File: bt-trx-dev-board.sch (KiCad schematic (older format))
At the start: 10 parts, among them J2 PTT_BUTTON, J3 AudioJack2, J4 PTT_SELECT, J5 RJ45, J6 ENABLE_PTT_IN, U1 SILabs_WT32i

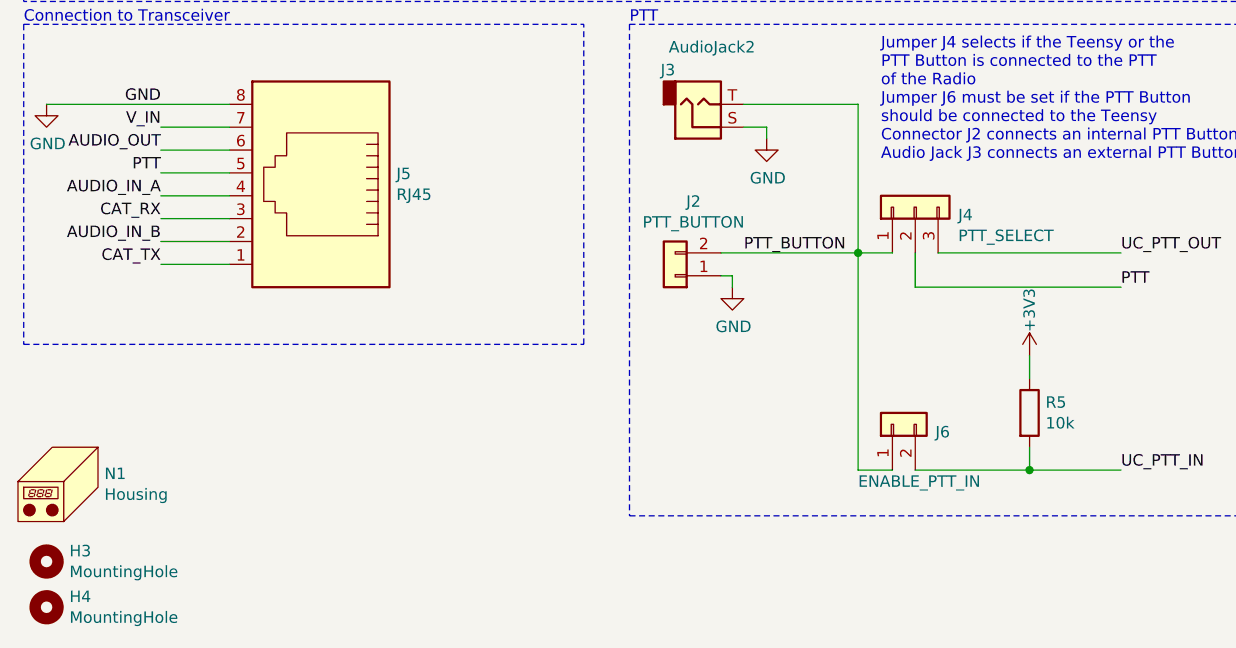
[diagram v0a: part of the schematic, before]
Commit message: Assigned Pins to ESP32 and removed Teensy [#1]
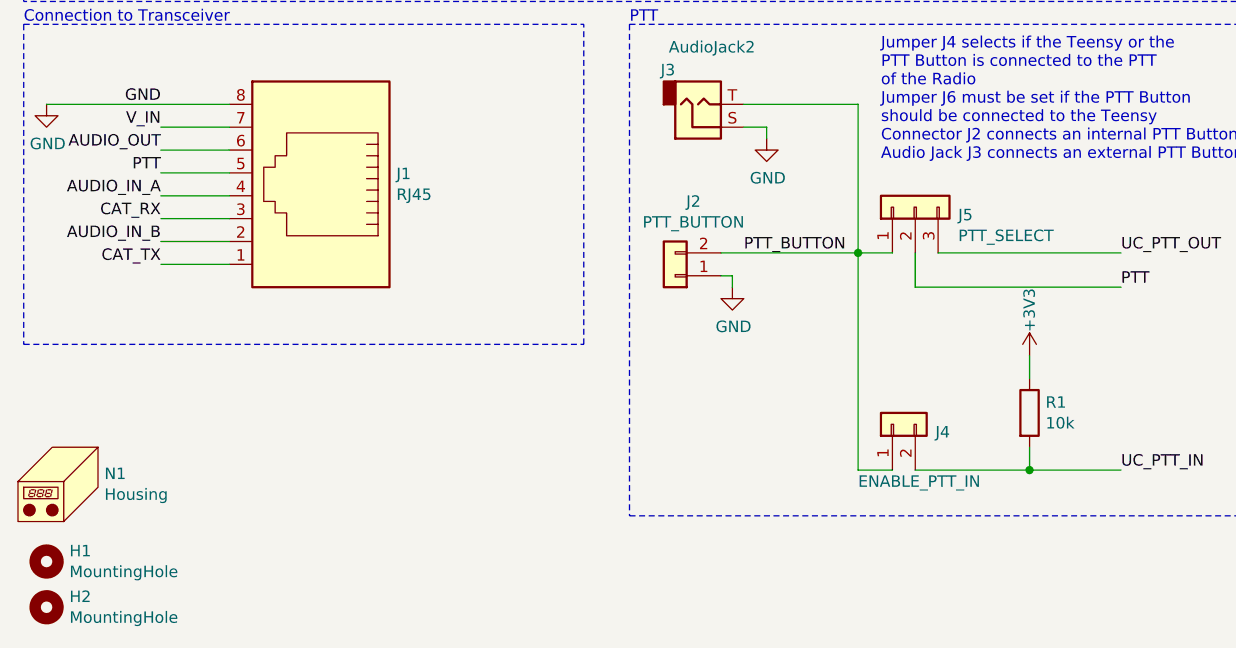
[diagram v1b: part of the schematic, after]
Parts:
- renumbered H3 to H1, H4 to H2, J5 to J1, J6 to J4, J4 to J5, R5 to R1
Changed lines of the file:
@@
 NoConn ~ 3950 3850
 $Comp
-L power:GND #PWR03
+L power:GND #PWR04
 U 1 1 5C05D773
 P 3150 3950
-F 0 "#PWR03" H 3150 3700 50  0001 C CNN
+F 0 "#PWR04" H 3150 3700 50  0001 C CNN
 F 1 "GND" H 3155 3777 50  0000 C CNN
 F 2 "" H 3150 3950 50  0001 C CNN
@@
 $EndComp
 $Comp
-L power:GND #PWR01
+L power:GND #PWR02
 U 1 1 5C05D830
 P 2600 1850
-F 0 "#PWR01" H 2600 1600 50  0001 C CNN
+F 0 "#PWR02" H 2600 1600 50  0001 C CNN
 F 1 "GND" H 2605 1677 50  0000 C CNN
 F 2 "" H 2600 1850 50  0001 C CNN
@@
 Connection ~ 2700 1850
 $Comp
-L power:GND #PWR04
+L power:GND #PWR07
 U 1 1 5C06905F
 P 4800 2550
-F 0 "#PWR04" H 4800 2300 50  0001 C CNN
+F 0 "#PWR07" H 4800 2300 50  0001 C CNN
 F 1 "GND" H 4805 2377 50  0000 C CNN
 F 2 "" H 4800 2550 50  0001 C CNN
@@
 MIC_BIAS
 $Comp
-L power:+3V3 #PWR02
+L power:+3V3 #PWR03
 U 1 1 5C08557D
 P 2750 3350
-F 0 "#PWR02" H 2750 3200 50  0001 C CNN
+F 0 "#PWR03" H 2750 3200 50  0001 C CNN
 F 1 "+3V3" H 2765 3523 50  0000 C CNN
 F 2 "" H 2750 3350 50  0001 C CNN
@@
 	4650 2750 4800 2750
 $Comp
-L power:+3V3 #PWR05
+L power:+3V3 #PWR08
 U 1 1 5C099E67
 P 4800 2750
-F 0 "#PWR05" H 4800 2600 50  0001 C CNN
+F 0 "#PWR08" H 4800 2600 50  0001 C CNN
 F 1 "+3V3" H 4815 2923 50  0000 C CNN
 F 2 "" H 4800 2750 50  0001 C CNN
@@
 WT32_ONOFF_FROM_UC
 $Comp
-L power:GND #PWR06
+L power:GND #PWR09
 U 1 1 5C1C6304
 P 4800 3350
-F 0 "#PWR06" H 4800 3100 50  0001 C CNN
+F 0 "#PWR09" H 4800 3100 50  0001 C CNN
 F 1 "GND" H 4805 3177 50  0000 C CNN
 F 2 "" H 4800 3350 50  0001 C CNN
@@
 AUDIO_IN_B
 $Comp
-L power:GND #PWR09
+L power:GND #PWR05
 U 1 1 5C0EA10B
 P 3800 5950
-F 0 "#PWR09" H 3800 5700 50  0001 C CNN
+F 0 "#PWR05" H 3800 5700 50  0001 C CNN
 F 1 "GND" H 3805 5777 50  0000 C CNN
 F 2 "" H 3800 5950 50  0001 C CNN
@@
 $EndComp
 $Comp
-L Mechanical:MountingHole H3
+L Mechanical:MountingHole H1
 U 1 1 5C071389
 P 800 7150
-F 0 "H3" H 900 7196 50  0000 L CNN
+F 0 "H1" H 900 7196 50  0000 L CNN
 F 1 "MountingHole" H 900 7105 50  0000 L CNN
 F 2 "MountingHole:MountingHole_3.2mm_M3_DIN965" H 800 7150 50  0001 C CNN
@@
 $EndComp
 $Comp
-L Mechanical:MountingHole H4
+L Mechanical:MountingHole H2
 U 1 1 5C0713CD
 P 800 7350
-F 0 "H4" H 900 7396 50  0000 L CNN
+F 0 "H2" H 900 7396 50  0000 L CNN
 F 1 "MountingHole" H 900 7305 50  0000 L CNN
 F 2 "MountingHole:MountingHole_3.2mm_M3_DIN965" H 800 7350 50  0001 C CNN
@@
 	8850 800  8750 800
 $Comp
-L power:GND #PWR011
+L power:GND #PWR013
 U 1 1 5C781CAB
 P 8650 1850
-F 0 "#PWR011" H 8650 1600 50  0001 C CNN
+F 0 "#PWR013" H 8650 1600 50  0001 C CNN
 F 1 "GND" H 8655 1677 50  0000 C CNN
 F 2 "" H 8650 1850 50  0001 C CNN
@@
 	8650 1750 8650 1850
 $Comp
-L power:GND #PWR07
+L power:GND #PWR010
 U 1 1 5C783418
 P 4850 1650
-F 0 "#PWR07" H 4850 1400 50  0001 C CNN
+F 0 "#PWR010" H 4850 1400 50  0001 C CNN
 F 1 "GND" H 4855 1477 50  0000 C CNN
 F 2 "" H 4850 1650 50  0001 C CNN
@@
 $EndComp
 $Comp
-L power:GND #PWR08
+L power:GND #PWR011
 U 1 1 5C78347E
 P 4850 2150
-F 0 "#PWR08" H 4850 1900 50  0001 C CNN
+F 0 "#PWR011" H 4850 1900 50  0001 C CNN
 F 1 "GND" H 4855 1977 50  0000 C CNN
 F 2 "" H 4850 2150 50  0001 C CNN
@@
 CAT_RX
 $Comp
-L Connector_Generic:Conn_01x03 J4
+L Connector_Generic:Conn_01x03 J5
 U 1 1 5C7B53A0
 P 4600 5600
-F 0 "J4" V 4566 5412 50  0000 R CNN
+F 0 "J5" V 4566 5412 50  0000 R CNN
 F 1 "PTT_SELECT" V 4475 5412 50  0000 R CNN
 F 2 "Connector_PinHeader_2.54mm:PinHeader_1x03_P2.54mm_Vertical" H 4600 5600 50  0001 C CNN
@@
 	4350 5800 4500 5800
 $Comp
-L power:GND #PWR010
+L power:GND #PWR06
 U 1 1 5C7A36F0
 P 3950 5300
-F 0 "#PWR010" H 3950 5050 50  0001 C CNN
+F 0 "#PWR06" H 3950 5050 50  0001 C CNN
 F 1 "GND" H 3955 5127 50  0000 C CNN
 F 2 "" H 3950 5300 50  0001 C CNN
@@
 	4350 5150 4350 5800
 $Comp
-L power:GND #PWR012
+L power:GND #PWR01
 U 1 1 5C038459
 P 800 5150
-F 0 "#PWR012" H 800 4900 50  0001 C CNN
+F 0 "#PWR01" H 800 4900 50  0001 C CNN
 F 1 "GND" H 805 4977 50  0000 C CNN
 F 2 "" H 800 5150 50  0001 C CNN
@@
 	8850 900  8750 900
 $Comp
-L Connector:RJ45 J5
+L Connector:RJ45 J1
 U 1 1 5C7A0AB1
 P 2000 5550
-F 0 "J5" H 1670 5646 50  0000 R CNN
+F 0 "J1" H 1670 5646 50  0000 R CNN
 F 1 "RJ45" H 1670 5555 50  0000 R CNN
 F 2 "Connector_RJ:RJ45_Amphenol_54602-x08_Horizontal" V 2000 5575 50  0001 C CNN
@@
 	2850 1750 2500 1750
 $Comp
-L power:+3V3 #PWR0101
+L power:+3V3 #PWR012
 U 1 1 5CD1BCEE
 P 5100 6250
-AR Path="/5CD1BCEE" Ref="#PWR0101"  Part="1"
+AR Path="/5CD1BCEE" Ref="#PWR012"  Part="1"
 AR Path="/5C10B93A/5CD1BCEE" Ref="#PWR?"  Part="1"
-F 0 "#PWR0101" H 5100 6100 50  0001 C CNN
+F 0 "#PWR012" H 5100 6100 50  0001 C CNN
 F 1 "+3V3" V 5100 6450 50  0000 C CNN
 F 2 "" H 5100 6250 50  0001 C CNN
@@
 $EndComp
 $Comp
-L Device:R R5
+L Device:R R1
 U 1 1 5CD1BCF6
 P 5100 6500
-AR Path="/5CD1BCF6" Ref="R5"  Part="1"
+AR Path="/5CD1BCF6" Ref="R1"  Part="1"
 AR Path="/5C10B93A/5CD1BCF6" Ref="R?"  Part="1"
-F 0 "R5" H 5170 6546 50  0000 L CNN
+F 0 "R1" H 5170 6546 50  0000 L CNN
 F 1 "10k" H 5170 6455 50  0000 L CNN
 F 2 "Resistor_SMD:R_0805_2012Metric_Pad1.15x1.40mm_HandSolder" V 5030 6500 50  0001 C CNN
@@
 P 4500 6550
 AR Path="/5C10B93A/5CD1BD02" Ref="J?"  Part="1"
-AR Path="/5CD1BD02" Ref="J6"  Part="1"
-F 0 "J6" V 4466 6362 50  0000 R CNN
+AR Path="/5CD1BD02" Ref="J4"  Part="1"
+F 0 "J4" V 4466 6362 50  0000 R CNN
 F 1 "ENABLE_PTT_IN" V 4250 6700 50  0000 R CNN
 F 2 "Connector_PinHeader_2.54mm:PinHeader_1x02_P2.54mm_Vertical" H 4500 6550 50  0001 C CNN

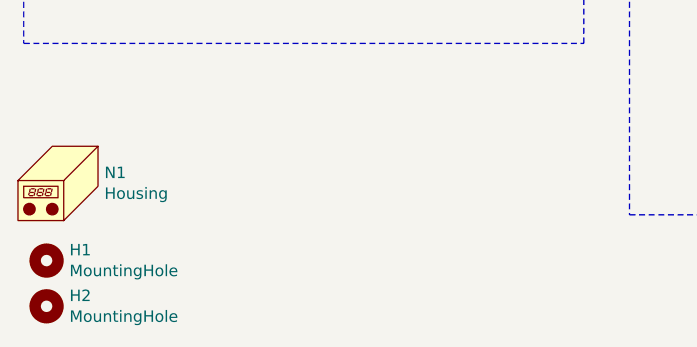
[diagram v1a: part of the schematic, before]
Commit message: Continued v4 [#1]
*removed all v3 stuff
* Resized board to max case size
* First deratsnesting
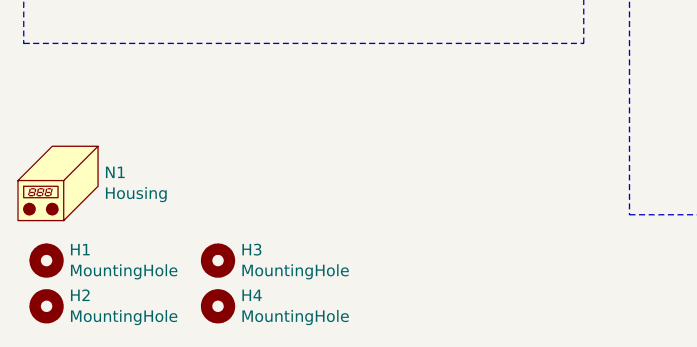
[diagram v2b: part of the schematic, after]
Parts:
- added H3, H4: MountingHole, MountingHole:MountingHole_3.2mm_M3_DIN965, symbol Mechanical:MountingHole
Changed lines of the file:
@@
 Wire Notes Line
 	3350 4800 6300 4800
+$Comp
+L Mechanical:MountingHole H3
+U 1 1 5D3AD2F8
+P 1550 7150
+F 0 "H3" H 1650 7196 50  0000 L CNN
+F 1 "MountingHole" H 1650 7105 50  0000 L CNN
+F 2 "MountingHole:MountingHole_3.2mm_M3_DIN965" H 1550 7150 50  0001 C CNN
+F 3 "~" H 1550 7150 50  0001 C CNN
+F 4 "-" H 750 0   50  0001 C CNN "Mouser Best.Nr."
+	1    1550 7150
+	1    0    0    -1
+$EndComp
+$Comp
+L Mechanical:MountingHole H4
+U 1 1 5D3AD300
+P 1550 7350
+F 0 "H4" H 1650 7396 50  0000 L CNN
+F 1 "MountingHole" H 1650 7305 50  0000 L CNN
+F 2 "MountingHole:MountingHole_3.2mm_M3_DIN965" H 1550 7350 50  0001 C CNN
+F 3 "~" H 1550 7350 50  0001 C CNN
+F 4 "-" H 750 0   50  0001 C CNN "Mouser Best.Nr."
+	1    1550 7350
+	1    0    0    -1
+$EndComp
 $EndSCHEMATC

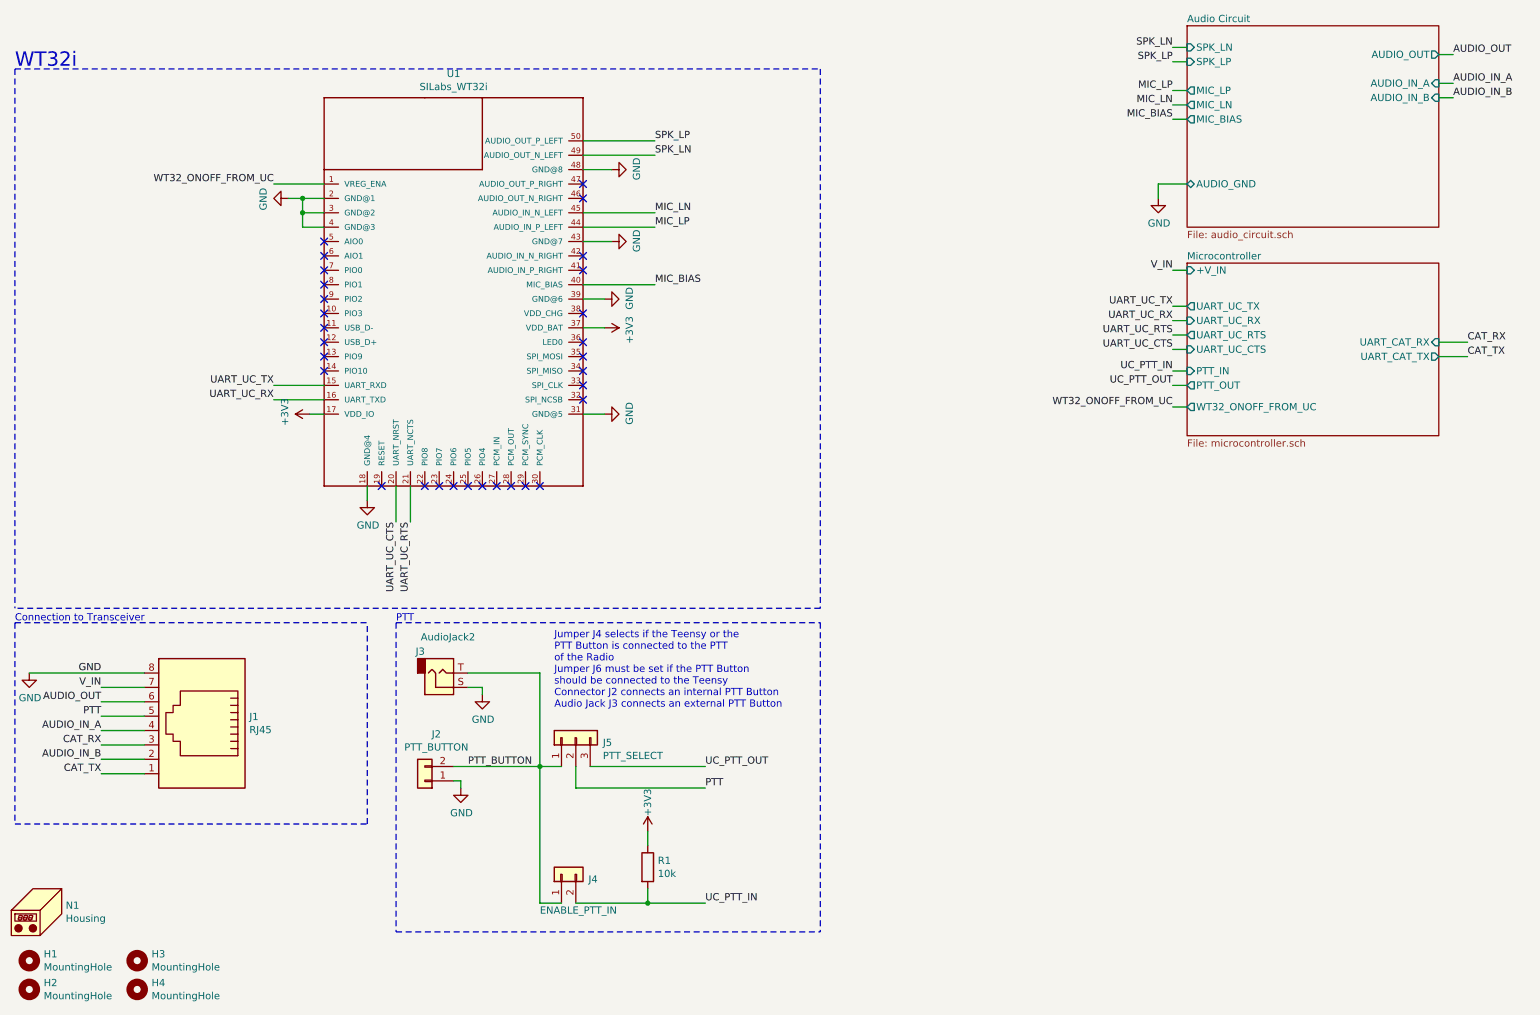
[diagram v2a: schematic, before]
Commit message: [#1] Refined Schematic
* Removed RTS CTS
* Added 15pF capacitator to audio IN+
* Removed PTT jumper
* Added pull-up jumper
* Added solder jmpr bypass to RV
* Changed button footprint to SMD version
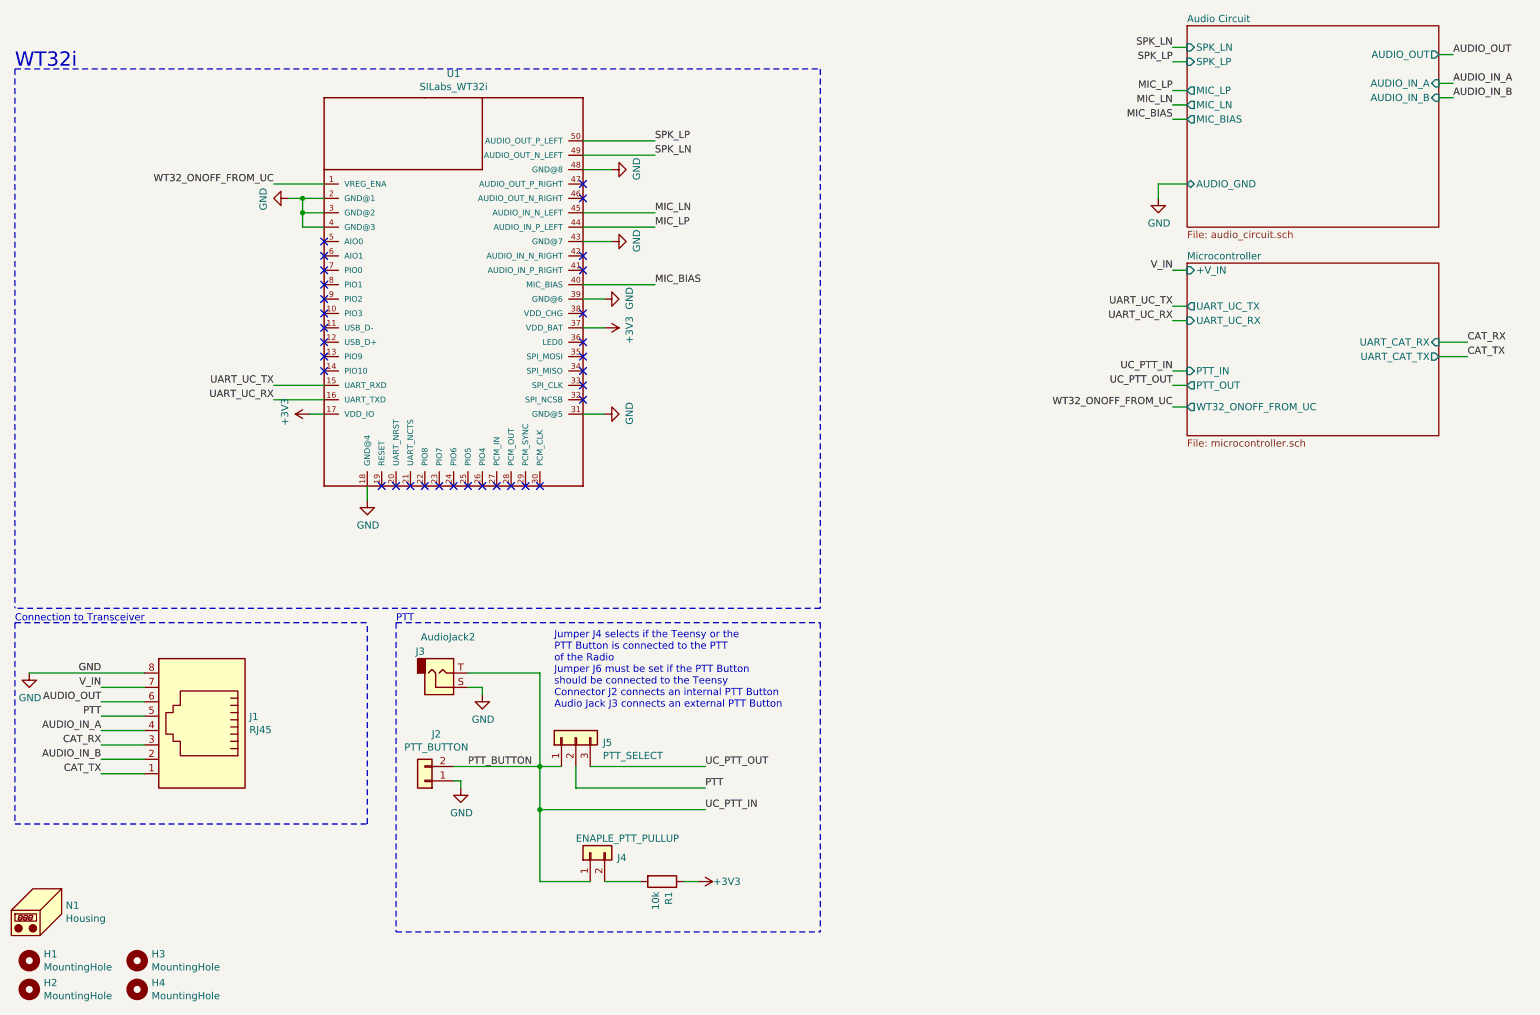
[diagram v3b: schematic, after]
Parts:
- J4: value ENABLE_PTT_IN -> ENAPLE_PTT_PULLUP
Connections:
- net UART_UC_CTS: no longer names the net of U1.20 (UART_NRST)
- net UART_UC_RTS: no longer names the net of U1.21 (UART_NCTS)
- net UC_PTT_IN: no longer names the net of J4.2 (Pin_2), R1.2
- no-connect marks 30 -> 32
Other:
- moved on the sheet: J4, R1
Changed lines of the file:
@@
 EESchema Schematic File Version 4
 LIBS:bt-trx-dev-board-cache
-EELAYER 26 0
+EELAYER 29 0
 EELAYER END
 $Descr A4 11693 8268
@@
 F 2 "Connector_PinHeader_2.54mm:PinHeader_1x02_P2.54mm_Vertical" H 3550 5900 50  0001 C CNN
 F 3 "~" H 3550 5900 50  0001 C CNN
-F 4 "" H 3550 5900 50  0001 C CNN "Reichelt Best.Nr."
-F 5 "855-M20-9990246" H -2300 -200 50  0001 C CNN "Mouser Best.Nr."
+F 4 "855-M20-9990246" H -2300 -200 50  0001 C CNN "Mouser Best.Nr."
 	1    3550 5900
 	-1   0    0    1
@@
 	1    0    0    -1
 $EndComp
-Wire Wire Line
-	3350 3850 3350 4100
-Wire Wire Line
-	3450 3850 3450 4100
-Text Label 3450 4100 3    50   ~ 0
-UART_UC_RTS
-Text Label 3350 4100 3    50   ~ 0
-UART_UC_CTS
 Wire Notes Line
 	700  950  700  4700
 Wire Notes Line
 	6300 950  6300 4700
-Wire Wire Line
-	8850 2800 8750 2800
-Wire Wire Line
-	8850 2900 8750 2900
-Text Label 8750 2800 2    50   ~ 0
-UART_UC_RTS
-Text Label 8750 2900 2    50   ~ 0
-UART_UC_CTS
 $Sheet
 S 8850 650  1750 1400
@@
 F4 "WT32_ONOFF_FROM_UC" O L 8850 3300 50
 F5 "+V_IN" I L 8850 2350 50
-F6 "UART_UC_RTS" O L 8850 2800 50
-F7 "UART_UC_CTS" I L 8850 2900 50
-F8 "UART_CAT_RX" I R 10600 2850 50
-F9 "UART_CAT_TX" O R 10600 2950 50
-F10 "PTT_IN" I L 8850 3050 50
-F11 "PTT_OUT" O L 8850 3150 50
+F6 "UART_CAT_RX" I R 10600 2850 50
+F7 "UART_CAT_TX" O R 10600 2950 50
+F8 "PTT_IN" I L 8850 3050 50
+F9 "PTT_OUT" O L 8850 3150 50
 $EndSheet
 Wire Wire Line
@@
 L power:+3V3 #PWR012
 U 1 1 5CD1BCEE
-P 5100 6250
+P 5450 6600
 AR Path="/5CD1BCEE" Ref="#PWR012"  Part="1"
 AR Path="/5C10B93A/5CD1BCEE" Ref="#PWR?"  Part="1"
-F 0 "#PWR012" H 5100 6100 50  0001 C CNN
-F 1 "+3V3" V 5100 6450 50  0000 C CNN
-F 2 "" H 5100 6250 50  0001 C CNN
-F 3 "" H 5100 6250 50  0001 C CNN
-	1    5100 6250
-	1    0    0    -1
+F 0 "#PWR012" H 5450 6450 50  0001 C CNN
+F 1 "+3V3" V 5450 6800 50  0000 C CNN
+F 2 "" H 5450 6600 50  0001 C CNN
+F 3 "" H 5450 6600 50  0001 C CNN
+	1    5450 6600
+	0    1    1    0
 $EndComp
 $Comp
 L Device:R R1
 U 1 1 5CD1BCF6
-P 5100 6500
+P 5200 6600
 AR Path="/5CD1BCF6" Ref="R1"  Part="1"
 AR Path="/5C10B93A/5CD1BCF6" Ref="R?"  Part="1"
-F 0 "R1" H 5170 6546 50  0000 L CNN
-F 1 "10k" H 5170 6455 50  0000 L CNN
-F 2 "Resistor_SMD:R_0805_2012Metric_Pad1.15x1.40mm_HandSolder" V 5030 6500 50  0001 C CNN
-F 3 "~" H 5100 6500 50  0001 C CNN
-F 4 "" H 1450 1350 50  0001 C CNN "Reichelt Best.Nr."
-F 5 "603-RC0805FR-0710KL" H 1450 1350 50  0001 C CNN "Mouser Best.Nr."
-	1    5100 6500
-	1    0    0    -1
-$EndComp
-Wire Wire Line
-	5100 6250 5100 6350
+F 0 "R1" H 5270 6646 50  0000 L CNN
+F 1 "10k" H 5270 6555 50  0000 L CNN
+F 2 "Resistor_SMD:R_0805_2012Metric_Pad1.15x1.40mm_HandSolder" V 5130 6600 50  0001 C CNN
+F 3 "~" H 5200 6600 50  0001 C CNN
+F 4 "603-RC0805FR-0710KL" H 1550 1450 50  0001 C CNN "Mouser Best.Nr."
+	1    5200 6600
+	0    1    1    0
+$EndComp
+Wire Wire Line
+	5450 6600 5350 6600
 $Comp
 L Connector_Generic:Conn_01x02 J?
 U 1 1 5CD1BD02
-P 4500 6550
+P 4700 6400
 AR Path="/5C10B93A/5CD1BD02" Ref="J?"  Part="1"
 AR Path="/5CD1BD02" Ref="J4"  Part="1"
-F 0 "J4" V 4466 6362 50  0000 R CNN
-F 1 "ENABLE_PTT_IN" V 4250 6700 50  0000 R CNN
-F 2 "Connector_PinHeader_2.54mm:PinHeader_1x02_P2.54mm_Vertical" H 4500 6550 50  0001 C CNN
-F 3 "~" H 4500 6550 50  0001 C CNN
-F 4 "855-M20-9990246" H -1150 4850 50  0001 C CNN "Mouser Best.Nr."
-	1    4500 6550
+F 0 "J4" V 4666 6212 50  0000 R CNN
+F 1 "ENAPLE_PTT_PULLUP" V 4800 6500 50  0000 R CNN
+F 2 "Connector_PinHeader_2.54mm:PinHeader_1x02_P2.54mm_Vertical" H 4700 6400 50  0001 C CNN
+F 3 "~" H 4700 6400 50  0001 C CNN
+F 4 "855-M20-9990246" H -950 4700 50  0001 C CNN "Mouser Best.Nr."
+	1    4700 6400
 	0    -1   -1   0
 $EndComp
-Wire Wire Line
-	4350 5800 4350 6750
-Text Label 5500 6750 0    50   ~ 0
+Text Label 5500 6100 0    50   ~ 0
 UC_PTT_IN
-Wire Notes Line
-	6300 4800 6300 6950
-Wire Notes Line
-	3350 4800 3350 6950
-Wire Wire Line
-	4350 6750 4500 6750
-Wire Wire Line
-	4600 6750 5100 6750
-Wire Wire Line
-	5100 6650 5100 6750
-Connection ~ 5100 6750
-Wire Wire Line
-	5100 6750 5500 6750
 Text Notes 4450 5400 0    50   ~ 0
 Jumper J4 selects if the Teensy or the\nPTT Button is connected to the PTT\nof the Radio\nJumper J6 must be set if the PTT Button\nshould be connected to the Teensy\nConnector J2 connects an internal PTT Button\nAudio Jack J3 connects an external PTT Button
@@
 	1    0    0    -1
 $EndComp
+Wire Wire Line
+	5050 6600 4800 6600
+Wire Wire Line
+	4350 6600 4700 6600
+Wire Wire Line
+	4350 5800 4350 6100
+Wire Wire Line
+	5500 6100 4350 6100
+Connection ~ 4350 6100
+Wire Wire Line
+	4350 6100 4350 6600
+Wire Notes Line
+	6300 4800 6300 6950
+Wire Notes Line
+	3350 4800 3350 6950
+NoConn ~ 3350 3850
+NoConn ~ 3450 3850
 $EndSCHEMATC
